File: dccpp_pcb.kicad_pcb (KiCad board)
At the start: 2 copper layers, 101.6 x 63.5 mm, 70 parts, among them J1 USB_B_Micro, J10 OSTTC022162, J11 OSTTC022162, J12 OSTTC022162, J2 AVR-ISP-6, J3 OSTTC022162, J4 OSTTC022162, J5 OSTTC022162, J6 OSTTC022162, J7 OSTTC022162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

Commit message: Routing complete
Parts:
- moved C24 3.22 mm to (114.8, 129.9)
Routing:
- net /PROG_EN: track 46.9 -> 74.5 mm, vias 3 -> 4
- net +5V: track 96.1 -> 119.2 mm, vias 3 -> 5
- net /PROG: track 48.5 -> 49.6 mm
- net /D4: track 24.7 -> 25.5 mm
- net /OUT_EN: track 42.7 -> 43.4 mm
- net GND: track 127.5 -> 127.2 mm, vias 67 -> 73

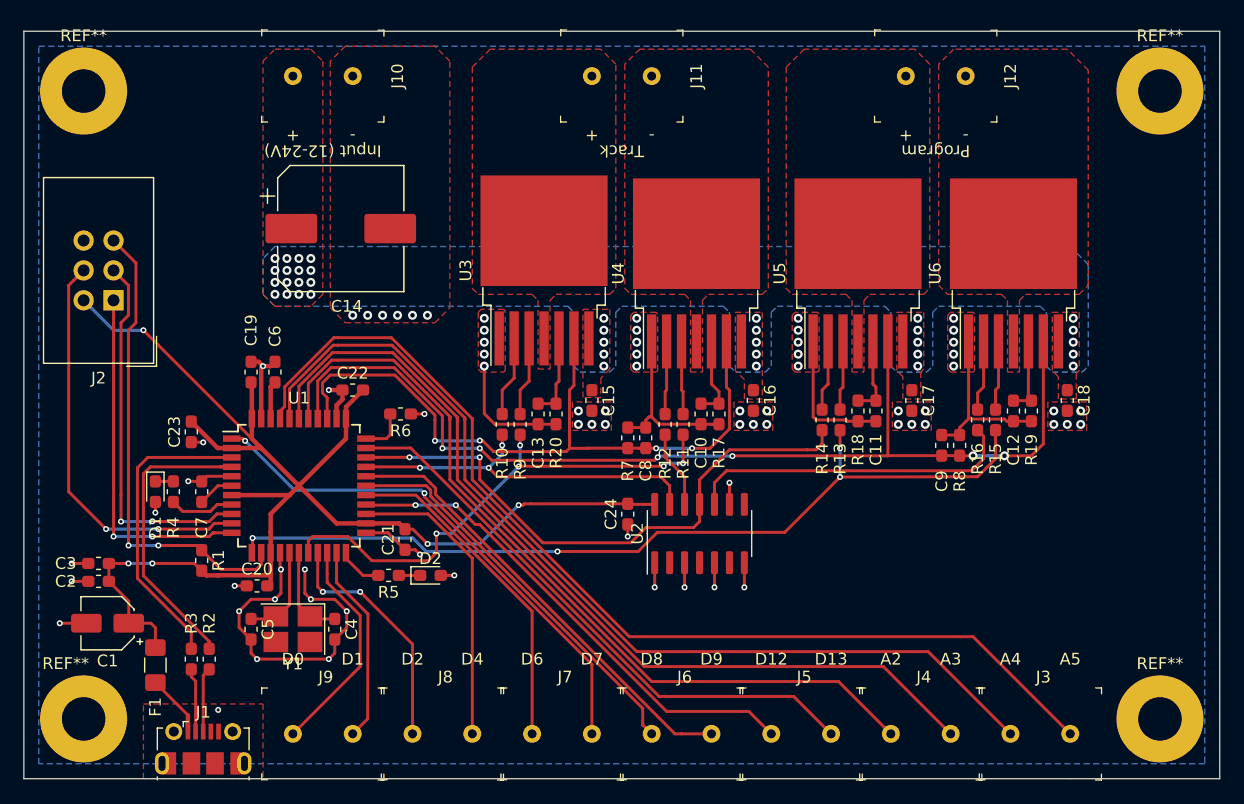
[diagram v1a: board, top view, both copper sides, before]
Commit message: Clean up silkscreen
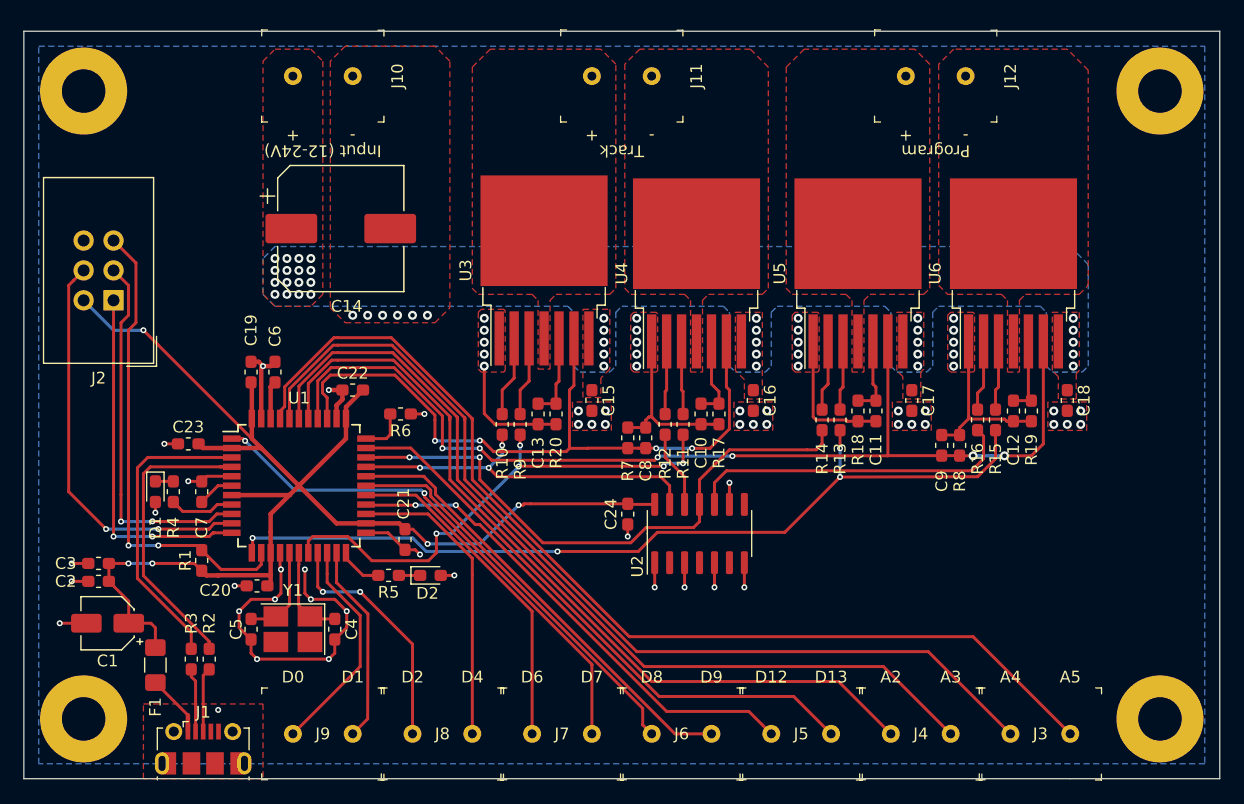
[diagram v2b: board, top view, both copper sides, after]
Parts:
- removed REF** (x2): MountingHole_3.7mm_Pad, MountingHole:MountingHole_3.7mm_Pad
- added ?: MountingHole_3.7mm_Pad, MountingHole:MountingHole_3.7mm_Pad, F.Cu at (68.6, 94.0)
- added ?: MountingHole_3.7mm_Pad, MountingHole:MountingHole_3.7mm_Pad, F.Cu at (160.0, 94.0)
- moved C23 1.05 mm to (77.5, 124.0), turned to 0 degrees
- renumbered REF** to ?
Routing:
- net +5V: track 119.2 -> 117.8 mm

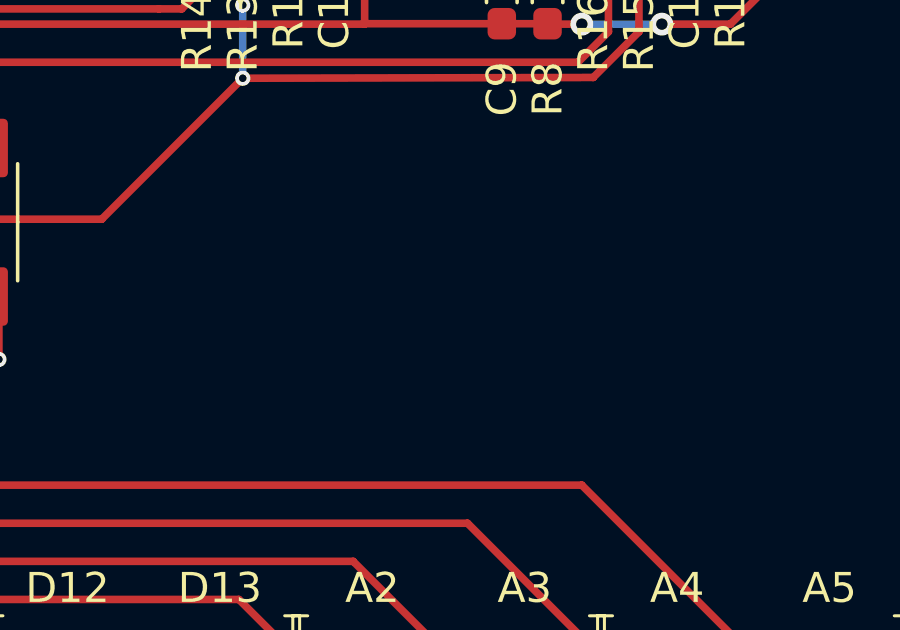
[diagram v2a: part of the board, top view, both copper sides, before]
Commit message: Add DCC logo
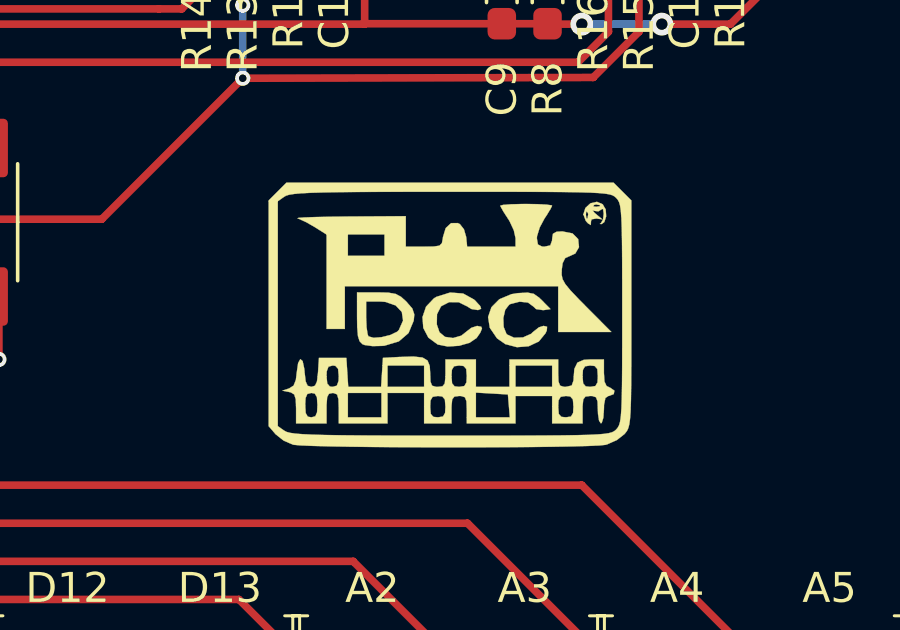
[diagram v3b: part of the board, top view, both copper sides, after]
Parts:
- added G***: LOGO, dccpp_pcb:nmra_dcc, F.Cu at (139.7, 134.6)

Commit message: Finished art
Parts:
- moved J10 0.13 mm to (91.6, 92.7)
- moved J11 0.13 mm to (117.0, 92.7)
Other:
- board text added: "DCC++"

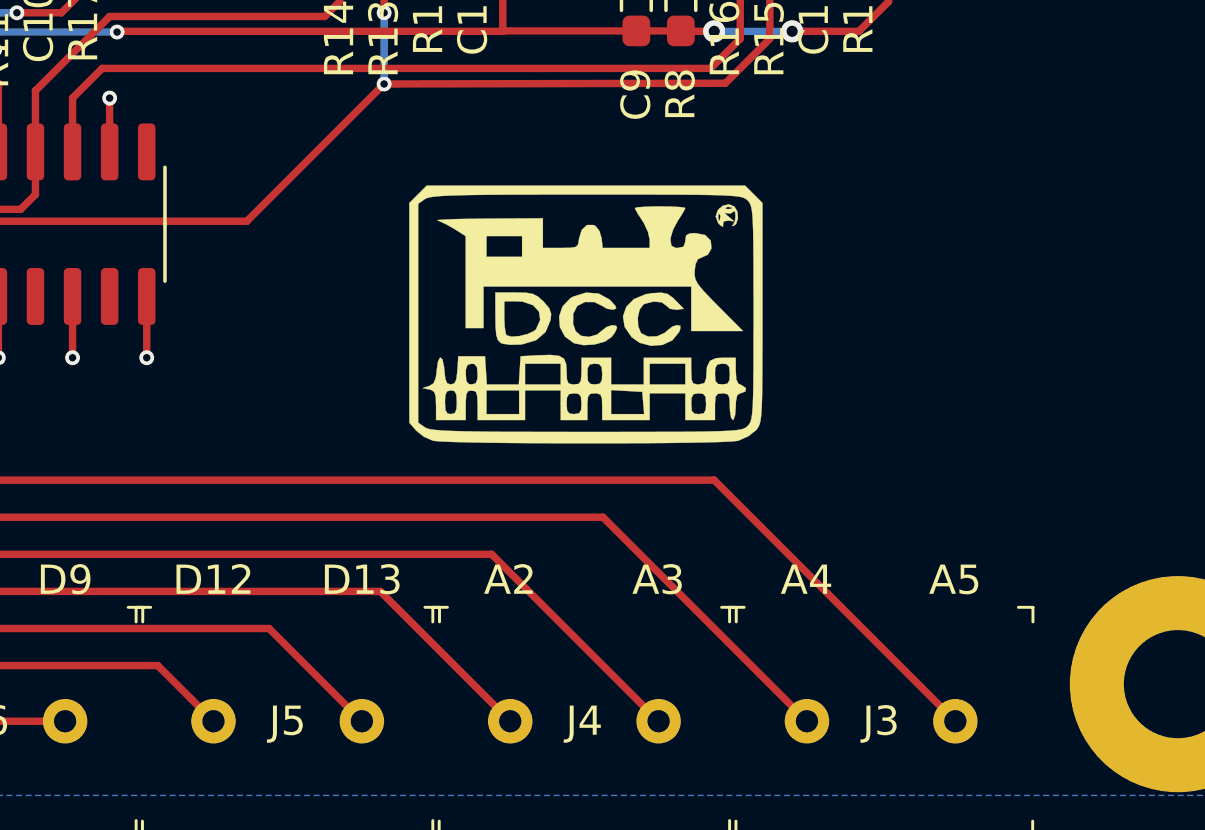
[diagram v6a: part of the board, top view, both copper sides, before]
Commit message: Clean up DCC logo
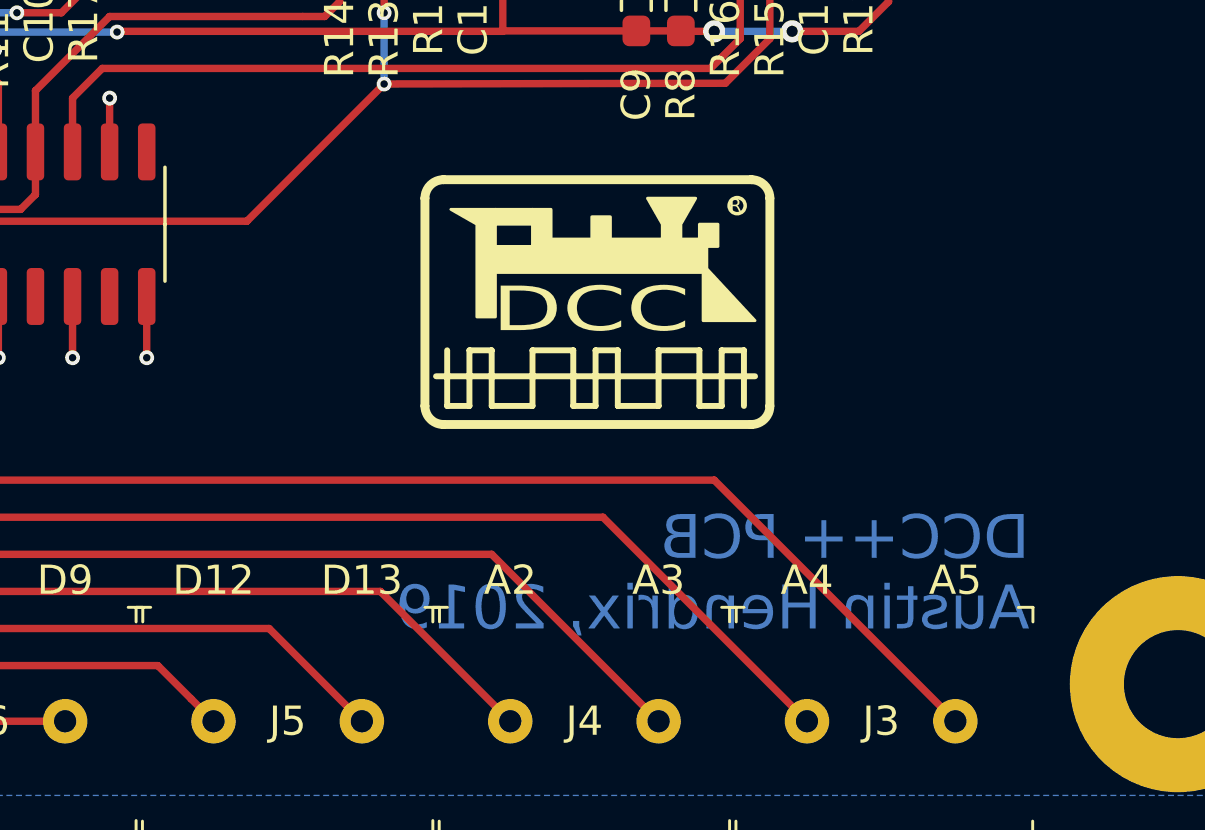
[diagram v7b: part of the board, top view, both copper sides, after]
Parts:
- removed G***: LOGO, dccpp_pcb:nmra_dcc
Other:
- board text added: "DCC"
- board text added: "DCC++ PCB Austin Hendrix, 2019"
- board text added: "R"

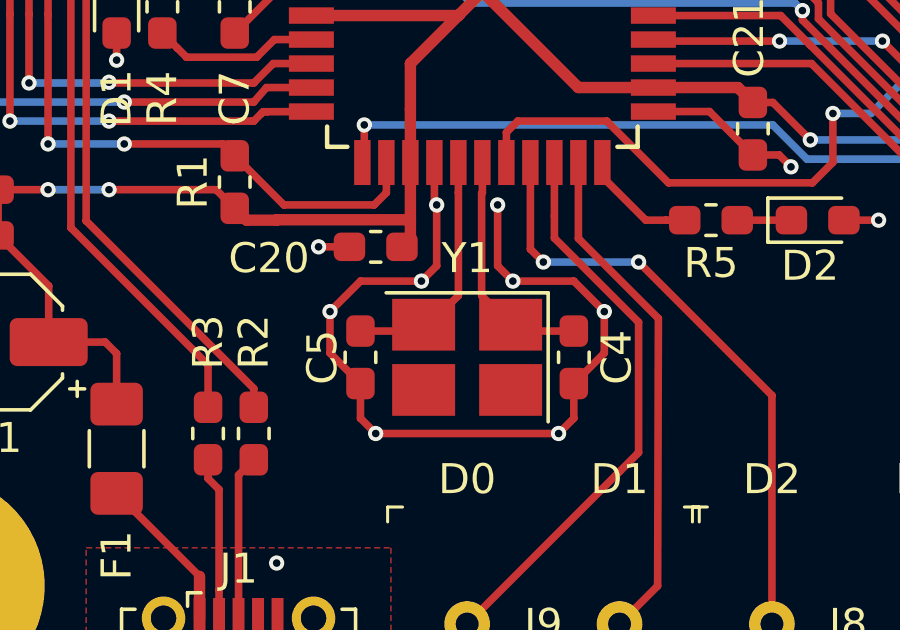
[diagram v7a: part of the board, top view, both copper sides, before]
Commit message: Fix crystal
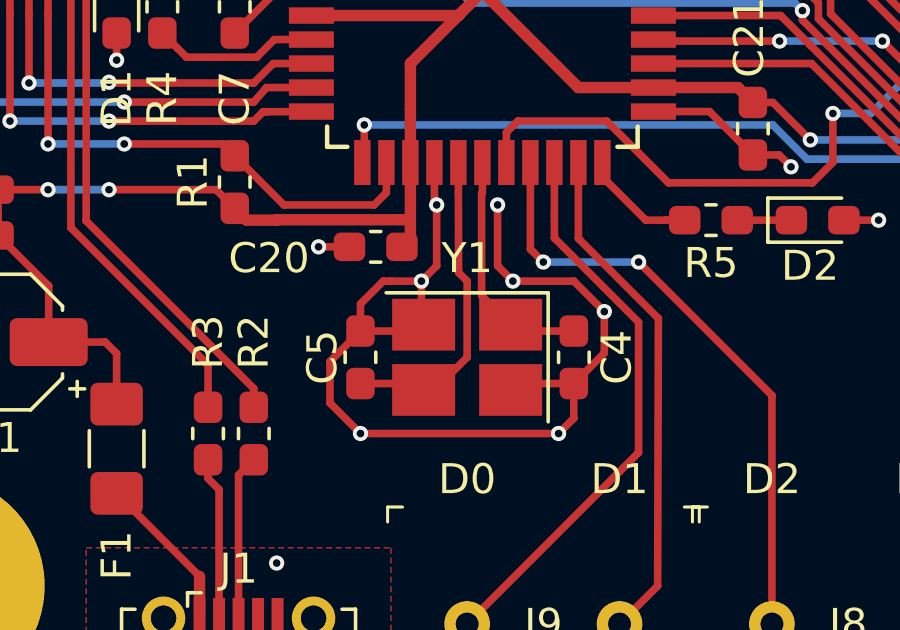
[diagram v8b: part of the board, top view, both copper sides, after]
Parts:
- turned C5 to 90 degrees
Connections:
- Y1 pad 2: Net-(C5-Pad1) -> GND
- Y1 pad 3: (no net) -> Net-(C5-Pad1)
- Y1 pad 4: (no net) -> GND
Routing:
- net GND: track 127.4 -> 133.3 mm, vias 73 -> 72
- net Net-(C5-Pad1): track 8.19 -> 10.7 mm
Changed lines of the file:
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@@
     (thickness 1.6)
     (drawings 686)
-    (tracks 654)
+    (tracks 662)
     (zones 0)
     (modules 70)
@@
   )
   (setup
-    (last_trace_width 0.1524)
+    (last_trace_width 0.254)
     (user_trace_width 0.1524)
     (user_trace_width 0.254)
@@
       (effects (font (size 0.7 0.7) (thickness 0.105)))
     )
-    (pad 4 smd rect (at -1.45 -1.0875 180) (size 2.1 1.725) (layers F.Cu F.Paste F.Mask))
-    (pad 3 smd rect (at 1.45 -1.0875 180) (size 2.1 1.725) (layers F.Cu F.Paste F.Mask))
-    (pad 2 smd rect (at 1.45 1.0875 180) (size 2.1 1.725) (layers F.Cu F.Paste F.Mask)
+    (pad 4 smd rect (at -1.45 -1.0875 180) (size 2.1 1.725) (layers F.Cu F.Paste F.Mask)
+      (net 1 GND))
+    (pad 3 smd rect (at 1.45 -1.0875 180) (size 2.1 1.725) (layers F.Cu F.Paste F.Mask)
       (net 4 "Net-(C5-Pad1)"))
+    (pad 2 smd rect (at 1.45 1.0875 180) (size 2.1 1.725) (layers F.Cu F.Paste F.Mask)
+      (net 1 GND))
     (pad 1 smd rect (at -1.45 1.0875 180) (size 2.1 1.725) (layers F.Cu F.Paste F.Mask)
       (net 3 "Net-(C4-Pad1)"))
@@
   )
   (module Capacitor_SMD:C_0603_1608Metric_Pad1.05x0.95mm_HandSolder (layer F.Cu)
-    (at 82.804 139.7 270)
+    (at 82.804 139.7 90)
     (descr "Capacitor SMD 0603 (1608 Metric), square (rectangular) end terminal, IPC_7351 nominal with elongated pad for handsoldering. (Body size source: http://www.tortai-tech.com/upload/download/2011102023233369053.pdf), generated with kicad-footprint-generator")
     (tags "capacitor handsolder")
     (attr smd)
-    (fp_text reference C5 (at 0 1.27 90) (layer F.SilkS)
+    (fp_text reference C5 (at 0 -1.27 90) (layer F.SilkS)
       (effects (font (size 1 1) (thickness 0.15)))
     )
-    (fp_text value "22pF 10V" (at 0 1.43 90) (layer F.Fab)
+    (fp_text value "22pF 10V" (at 0 1.43 -90) (layer F.Fab)
       (effects (font (size 1 1) (thickness 0.15)))
     )
-    (fp_text user %R (at 0 0 90) (layer F.Fab)
+    (fp_text user %R (at 0 0 -90) (layer F.Fab)
       (effects (font (size 0.4 0.4) (thickness 0.06)))
     )
@@
     (fp_line (start -0.8 -0.4) (end 0.8 -0.4) (layer F.Fab) (width 0.1))
     (fp_line (start -0.8 0.4) (end -0.8 -0.4) (layer F.Fab) (width 0.1))
-    (pad 2 smd roundrect (at 0.875 0 270) (size 1.05 0.95) (layers F.Cu F.Paste F.Mask) (roundrect_rratio 0.25)
+    (pad 2 smd roundrect (at 0.875 0 90) (size 1.05 0.95) (layers F.Cu F.Paste F.Mask) (roundrect_rratio 0.25)
       (net 1 GND))
-    (pad 1 smd roundrect (at -0.875 0 270) (size 1.05 0.95) (layers F.Cu F.Paste F.Mask) (roundrect_rratio 0.25)
+    (pad 1 smd roundrect (at -0.875 0 90) (size 1.05 0.95) (layers F.Cu F.Paste F.Mask) (roundrect_rratio 0.25)
       (net 4 "Net-(C5-Pad1)"))
     (model ${KISYS3DMOD}/Capacitor_SMD.3dshapes/C_0603_1608Metric.wrl
@@
   (segment (start 90.932 138.176) (end 90.932 138.176) (width 0.1524) (layer F.Cu) (net 1))
   (via (at 90.932 138.176) (size 0.508) (drill 0.254) (layers F.Cu B.Cu) (net 1))
-  (segment (start 81.788 138.176) (end 81.788 138.176) (width 0.1524) (layer F.Cu) (net 1))
-  (via (at 81.788 138.176) (size 0.508) (drill 0.254) (layers F.Cu B.Cu) (net 1))
-  (via (at 83.312 142.24) (size 0.508) (drill 0.254) (layers F.Cu B.Cu) (net 1))
   (segment (start 89.408 142.24) (end 89.408 142.24) (width 0.1524) (layer F.Cu) (net 1))
   (via (at 89.408 142.24) (size 0.508) (drill 0.254) (layers F.Cu B.Cu) (net 1))
@@
   (segment (start 89.916 141.732) (end 89.408 142.24) (width 0.254) (layer F.Cu) (net 1))
   (segment (start 89.916 140.575) (end 89.916 141.732) (width 0.254) (layer F.Cu) (net 1))
-  (segment (start 89.408 142.24) (end 83.312 142.24) (width 0.254) (layer F.Cu) (net 1))
-  (segment (start 82.804 141.732) (end 82.804 140.575) (width 0.254) (layer F.Cu) (net 1))
-  (segment (start 82.804 141.732) (end 83.312 142.24) (width 0.254) (layer F.Cu) (net 1))
-  (segment (start 81.788 139.559) (end 81.788 138.176) (width 0.254) (layer F.Cu) (net 1))
-  (segment (start 82.804 140.575) (end 81.788 139.559) (width 0.254) (layer F.Cu) (net 1))
-  (segment (start 82.804 137.16) (end 84.836 137.16) (width 0.254) (layer F.Cu) (net 1))
-  (segment (start 81.788 138.176) (end 82.804 137.16) (width 0.254) (layer F.Cu) (net 1))
   (segment (start 84.836 137.16) (end 85.344 136.652) (width 0.254) (layer F.Cu) (net 1))
   (segment (start 85.344 136.652) (end 85.344 134.62) (width 0.254) (layer F.Cu) (net 1))
@@
   (via (at 75.438 123.952) (size 0.508) (drill 0.254) (layers F.Cu B.Cu) (net 1))
   (segment (start 75.438 123.952) (end 76.595 123.952) (width 0.254) (layer F.Cu) (net 1))
+  (via (at 82.804 142.24) (size 0.508) (drill 0.254) (layers F.Cu B.Cu) (net 1))
+  (segment (start 89.408 142.24) (end 82.804 142.24) (width 0.254) (layer F.Cu) (net 1))
   (segment (start 90.868 120.827) (end 92.315 119.38) (width 0.381) (layer F.Cu) (net 2))
   (segment (start 90.868 121.808) (end 90.868 120.827) (width 0.381) (layer F.Cu) (net 2))
@@
   (segment (start 88.0225 138.825) (end 87.81 138.6125) (width 0.254) (layer F.Cu) (net 3))
   (segment (start 89.916 138.825) (end 88.0225 138.825) (width 0.254) (layer F.Cu) (net 3))
-  (segment (start 84.6975 138.825) (end 84.91 138.6125) (width 0.254) (layer F.Cu) (net 4))
-  (segment (start 82.804 138.825) (end 84.6975 138.825) (width 0.254) (layer F.Cu) (net 4))
+  (segment (start 84.91 138.6125) (end 85.0975 138.6125) (width 0.254) (layer F.Cu) (net 1))
+  (segment (start 88.0225 140.575) (end 87.81 140.7875) (width 0.254) (layer F.Cu) (net 1))
+  (segment (start 89.916 140.575) (end 88.0225 140.575) (width 0.254) (layer F.Cu) (net 1))
+  (segment (start 84.836 138.5385) (end 84.91 138.6125) (width 0.254) (layer F.Cu) (net 1))
+  (segment (start 84.836 137.16) (end 84.836 138.5385) (width 0.254) (layer F.Cu) (net 1))
+  (segment (start 84.6975 138.825) (end 84.91 138.6125) (width 0.254) (layer F.Cu) (net 1))
+  (segment (start 82.804 138.825) (end 84.6975 138.825) (width 0.254) (layer F.Cu) (net 1))
+  (segment (start 82.804 142.24) (end 81.788 141.224) (width 0.254) (layer F.Cu) (net 1))
+  (segment (start 81.788 139.841) (end 82.804 138.825) (width 0.254) (layer F.Cu) (net 1))
+  (segment (start 81.788 141.224) (end 81.788 139.841) (width 0.254) (layer F.Cu) (net 1))
+  (segment (start 83.82 137.16) (end 84.836 137.16) (width 0.254) (layer F.Cu) (net 1))
+  (segment (start 83.566 137.16) (end 83.82 137.16) (width 0.254) (layer F.Cu) (net 1))
+  (segment (start 82.804 138.825) (end 82.804 137.922) (width 0.254) (layer F.Cu) (net 1))
+  (segment (start 82.804 137.922) (end 83.566 137.16) (width 0.254) (layer F.Cu) (net 1))
   (segment (start 86.068 134.212) (end 86.068 133.208) (width 0.254) (layer F.Cu) (net 4))
-  (segment (start 86.068 137.642) (end 86.068 134.212) (width 0.254) (layer F.Cu) (net 4))
-  (segment (start 85.0975 138.6125) (end 86.068 137.642) (width 0.254) (layer F.Cu) (net 4))
-  (segment (start 84.91 138.6125) (end 85.0975 138.6125) (width 0.254) (layer F.Cu) (net 4))
+  (segment (start 84.6975 140.575) (end 84.91 140.7875) (width 0.254) (layer F.Cu) (net 4))
+  (segment (start 82.804 140.575) (end 84.6975 140.575) (width 0.254) (layer F.Cu) (net 4))
+  (segment (start 84.91 140.7875) (end 85.2725 140.7875) (width 0.254) (layer F.Cu) (net 4))
+  (segment (start 85.2725 140.7875) (end 86.36 139.7) (width 0.254) (layer F.Cu) (net 4))
+  (segment (start 86.36 137.16) (end 86.075314 136.875314) (width 0.254) (layer F.Cu) (net 4))
+  (segment (start 86.36 139.7) (end 86.36 137.16) (width 0.254) (layer F.Cu) (net 4))
+  (segment (start 86.075314 136.875314) (end 86.068 134.212) (width 0.254) (layer F.Cu) (net 4))
   (segment (start 84.468 119.099) (end 84.836 118.731) (width 0.381) (layer F.Cu) (net 5))
   (segment (start 84.468 121.808) (end 84.468 119.099) (width 0.381) (layer F.Cu) (net 5))
